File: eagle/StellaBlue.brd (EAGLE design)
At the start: 108.9 x 85.8 mm, 89 parts, among them IC1 74LS245N, IC2 74LS245N, IC3 74LS245N, IC5 7805TV, T1 2N3906, T2 2N3904, T3 2N3906, T4 2N3904, X1 FMS6141

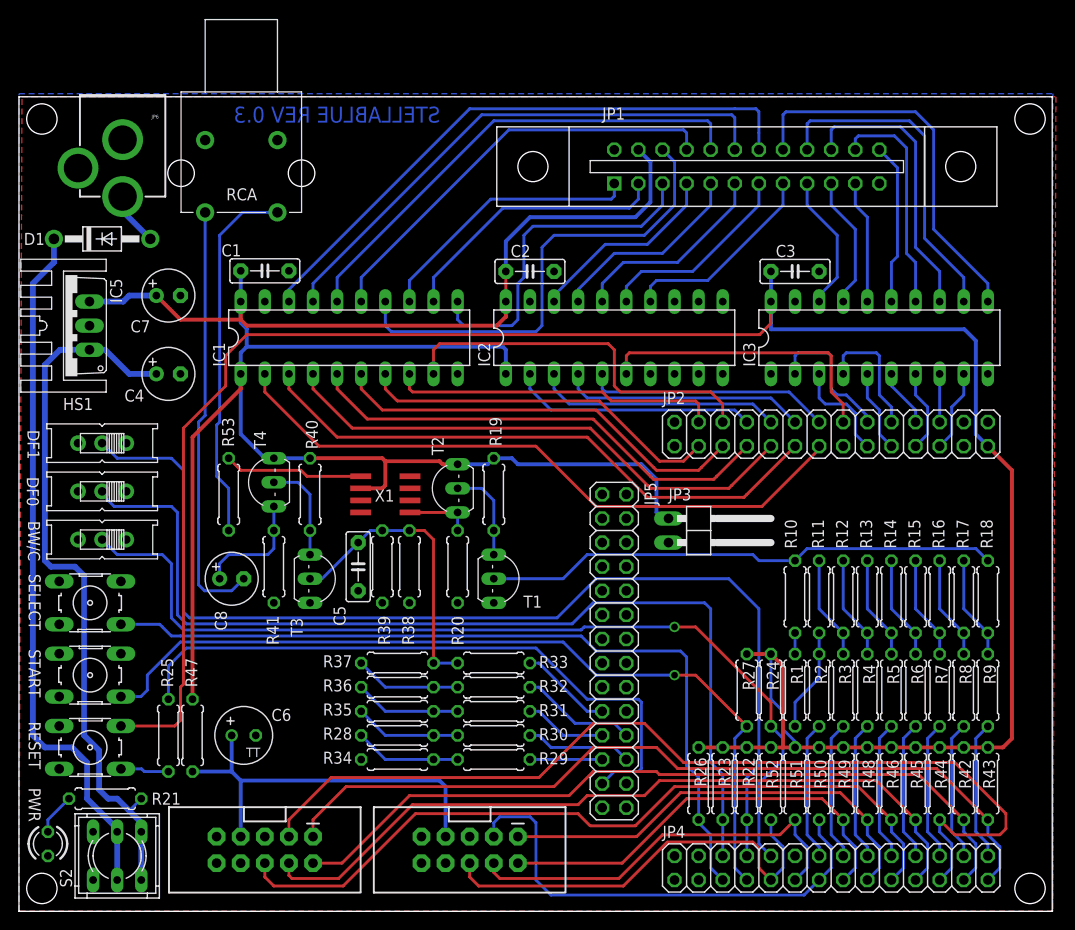
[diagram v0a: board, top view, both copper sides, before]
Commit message: First PCB routing !
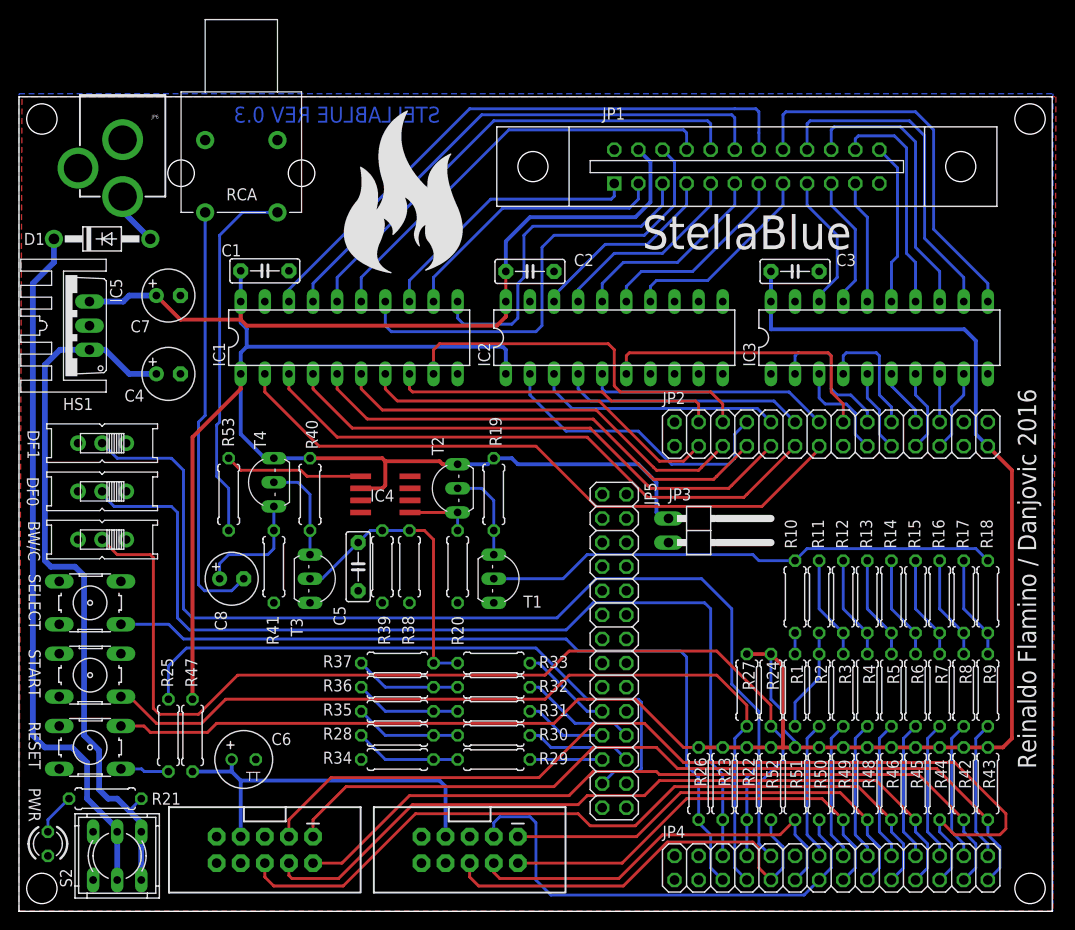
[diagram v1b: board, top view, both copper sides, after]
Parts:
- moved C6 2.54 mm to (23.2, 15.2)
- renumbered X1 to IC4
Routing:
- net +3V3: track 237.0 -> 193.6 mm
- net CL: track 99.5 -> 110.5 mm, vias 1 -> 0
- net N$30: track 25.9 -> 31.4 mm
- net J+5V: track 42.3 -> 39.8 mm
- net DF1: track 115.2 -> 113.3 mm
- net DF0: track 104.2 -> 104.9 mm
- net ST: track 90.2 -> 90.0 mm, vias 1 -> 0
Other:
- board text added: "Reinaldo Flamino / Danjovic 2016"
- board text added: "StellaBlue"

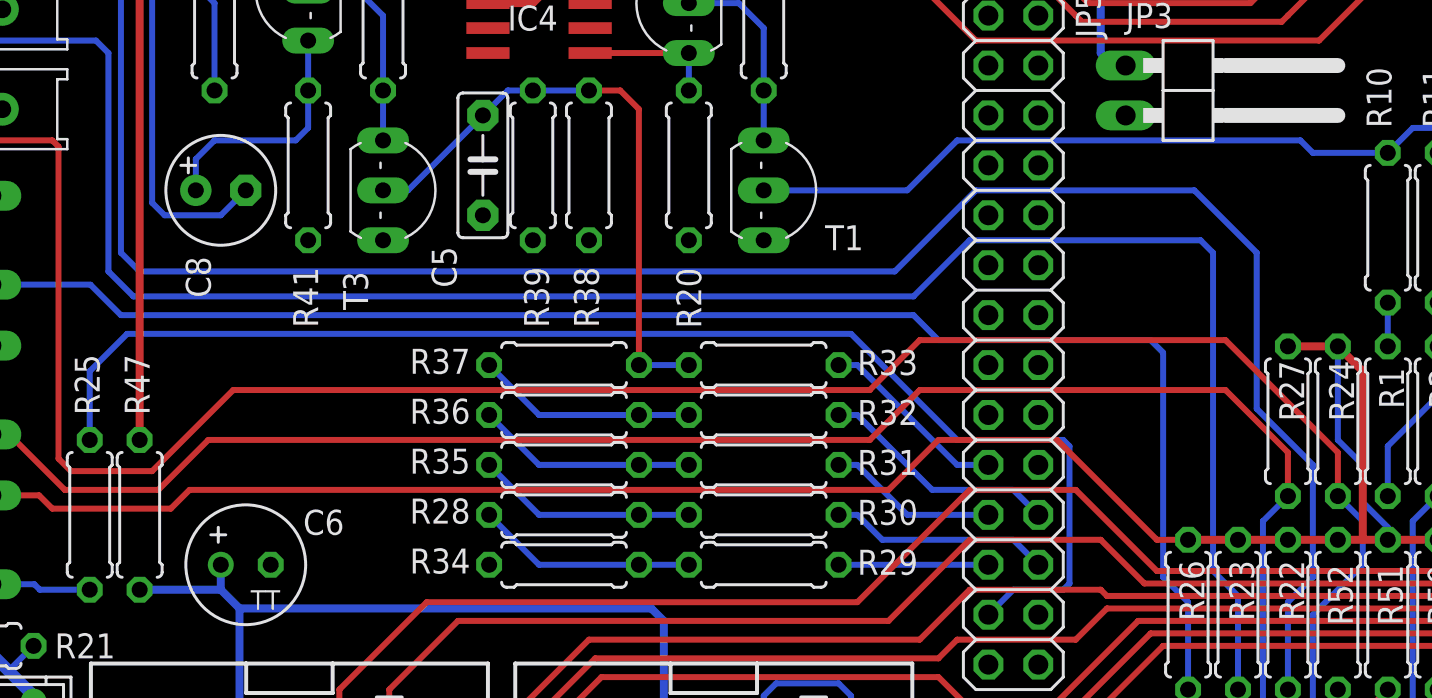
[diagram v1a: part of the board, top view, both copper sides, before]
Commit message: Added 14.318MHz crystal oscillator
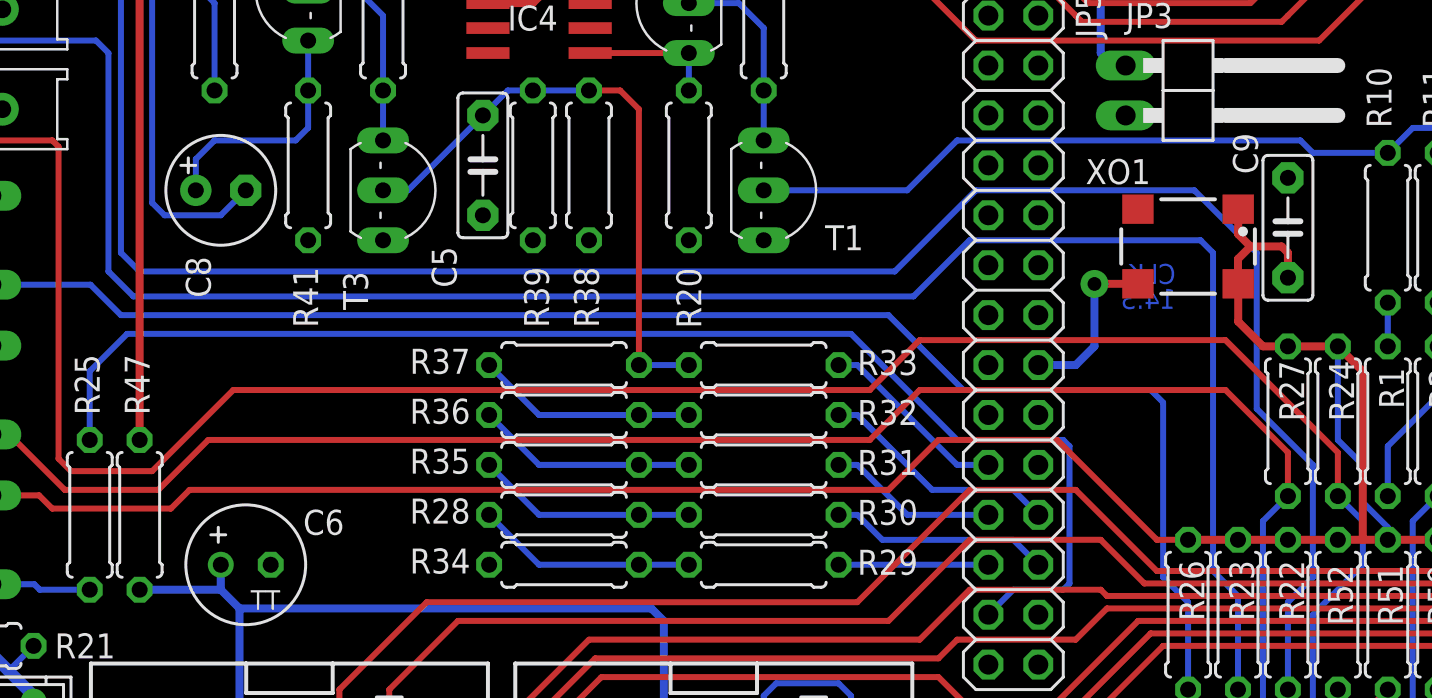
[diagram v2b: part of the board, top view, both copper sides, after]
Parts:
- added C9: 10nf, capacitor-wima:C5B2.5
- added XO1: 14.318MHz, crystal:SM77H
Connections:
- new net 14.318MHZ: JP5.16, XO1.3
- net +3V3: now also C9.1, XO1.1, XO1.4
- net GND: now also C9.2, XO1.2
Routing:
- net +3V3: track 193.6 -> 206.2 mm
- net 14.318MHZ: track 0.00 -> 8.64 mm, vias 0 -> 1
- net SL: track 86.1 -> 84.6 mm
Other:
- board text added: "14.3"
- board text added: "CLK"
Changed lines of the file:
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@@
 <?xml version="1.0" encoding="utf-8"?>
 <!DOCTYPE eagle SYSTEM "eagle.dtd">
-<eagle version="7.3.0">
+<eagle version="6.5.0">
 <drawing>
 <settings>
@@
 <rectangle x1="40.374503125" y1="83.61471875" x2="40.456615625" y2="83.6420875" layer="21"/>
 <text x="105.7275" y="34.29" size="1.9304" layer="21" font="vector" ratio="13" rot="R90" align="center">Reinaldo Flamino / Danjovic 2016</text>
+<text x="70.485" y="29.5275" size="1.016" layer="16" font="vector" ratio="15" rot="MR0">CLK</text>
+<text x="70.485" y="28.2575" size="1.016" layer="16" font="vector" ratio="15" rot="MR0">14.3</text>
 </plain>
 <attributes>
@@
 <pass name="Default">
 <param name="RoutingGrid" value="6.25mil"/>
-<param name="AutoGrid" value="1"/>
-<param name="Efforts" value="2"/>
-<param name="TopRouterVariant" value="1"/>
 <param name="tpViaShape" value="round"/>
 <param name="PrefDir.1" value="-"/>
@@
 <attribute name="VALUE" x="22.0345" y="30.988" size="1.27" layer="27" ratio="10" rot="R270"/>
 </element>
+<element name="XO1" library="crystal" package="SM77H" value="14.318MHz" x="71.12" y="31.4325" smashed="yes" rot="R180">
+<attribute name="NAME" x="69.215" y="35.8775" size="1.27" layer="25" rot="R180"/>
+<attribute name="VALUE" x="74.676" y="27.4955" size="1.27" layer="27" rot="R180"/>
+</element>
+<element name="C9" library="capacitor-wima" package="C5B2.5" value="10nf" x="76.2" y="32.385" smashed="yes" rot="R90">
+<attribute name="NAME" x="74.676" y="35.1155" size="1.27" layer="25" ratio="10" rot="R90"/>
+<attribute name="VALUE" x="78.994" y="30.353" size="1.27" layer="27" ratio="10" rot="R90"/>
+</element>
 </elements>
 <signals>
@@
 <contactref element="R1" pad="2"/>
 <wire x1="81.28" y1="28.575" x2="81.28" y2="26.3525" width="0.3048" layer="16"/>
+<contactref element="XO1" pad="2"/>
+<contactref element="XO1" pad="2"/>
+<contactref element="C9" pad="2"/>
 </signal>
 <signal name="N$49">
@@
 <wire x1="64.4525" y1="21.59" x2="69.5325" y2="16.51" width="0.3048" layer="1"/>
 <wire x1="69.5325" y1="16.51" x2="71.12" y2="16.51" width="0.3048" layer="1"/>
+<contactref element="XO1" pad="4"/>
+<contactref element="XO1" pad="1"/>
+<contactref element="C9" pad="1"/>
+<wire x1="73.67" y1="33.3325" x2="73.67" y2="32.0575" width="0.4064" layer="1"/>
+<wire x1="73.67" y1="32.0575" x2="74.295" y2="31.4325" width="0.4064" layer="1"/>
+<wire x1="74.295" y1="31.4325" x2="73.66" y2="30.7975" width="0.4064" layer="1"/>
+<wire x1="73.66" y1="30.7975" x2="73.66" y2="29.5425" width="0.4064" layer="1"/>
+<wire x1="73.66" y1="29.5425" x2="73.67" y2="29.5325" width="0.4064" layer="1"/>
+<wire x1="76.2" y1="31.115" x2="75.8825" y2="31.4325" width="0.4064" layer="1"/>
+<wire x1="75.8825" y1="31.4325" x2="74.295" y2="31.4325" width="0.4064" layer="1"/>
+<wire x1="76.2" y1="29.845" x2="76.2" y2="31.115" width="0.4064" layer="1"/>
+<wire x1="76.2" y1="26.3525" x2="74.93" y2="26.3525" width="0.4064" layer="1"/>
+<wire x1="73.67" y1="29.5325" x2="73.67" y2="27.6125" width="0.4064" layer="1"/>
+<wire x1="73.67" y1="27.6125" x2="74.93" y2="26.3525" width="0.4064" layer="1"/>
 </signal>
 <signal name="CL">
@@
 <wire x1="10.2362" y1="29.4894" x2="15.2781" y2="29.4894" width="0.3048" layer="16"/>
 <wire x1="15.2781" y1="29.4894" x2="16.8275" y2="27.94" width="0.3048" layer="16"/>
-<wire x1="16.8275" y1="27.94" x2="57.15" y2="27.94" width="0.3048" layer="16"/>
-<wire x1="57.15" y1="27.94" x2="58.42" y2="26.67" width="0.3048" layer="16"/>
-<wire x1="58.42" y1="26.67" x2="69.215" y2="26.67" width="0.3048" layer="16"/>
+<wire x1="16.8275" y1="27.94" x2="55.88" y2="27.94" width="0.3048" layer="16"/>
+<wire x1="55.88" y1="27.94" x2="59.69" y2="24.13" width="0.3048" layer="16"/>
+<wire x1="59.69" y1="24.13" x2="69.215" y2="24.13" width="0.3048" layer="16"/>
 <wire x1="71.12" y1="8.89" x2="71.12" y2="13.335" width="0.3048" layer="16"/>
 <wire x1="71.12" y1="13.335" x2="69.85" y2="14.605" width="0.3048" layer="16"/>
-<wire x1="69.85" y1="14.605" x2="69.85" y2="26.035" width="0.3048" layer="16"/>
-<wire x1="69.215" y1="26.67" x2="69.85" y2="26.035" width="0.3048" layer="16"/>
+<wire x1="69.85" y1="14.605" x2="69.85" y2="23.495" width="0.3048" layer="16"/>
+<wire x1="69.215" y1="24.13" x2="69.85" y2="23.495" width="0.3048" layer="16"/>
 </signal>
 <signal name="ST">
@@
 <wire x1="12.7" y1="13.97" x2="15.24" y2="13.97" width="0.3048" layer="16"/>
 </signal>
+<signal name="14.318MHZ">
+<contactref element="XO1" pad="3"/>
+<contactref element="JP5" pad="16"/>
+<wire x1="68.57" y1="29.5325" x2="66.3625" y2="29.5325" width="0.4064" layer="1"/>
+<wire x1="66.3625" y1="29.5325" x2="66.3575" y2="29.5275" width="0.4064" layer="1"/>
+<via x="66.3575" y="29.5275" extent="1-16" drill="0.7" diameter="1.4224"/>
+<wire x1="66.3575" y1="29.5275" x2="66.3575" y2="26.3525" width="0.4064" layer="16"/>
+<wire x1="66.3575" y1="26.3525" x2="65.405" y2="25.4" width="0.4064" layer="16"/>
+<wire x1="65.405" y1="25.4" x2="63.5" y2="25.4" width="0.4064" layer="16"/>
+</signal>
 </signals>
